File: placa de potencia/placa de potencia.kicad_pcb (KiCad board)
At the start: 2 copper layers, 125 x 121.6 mm, 21 parts, among them J1 XT60-M, J10 B4B-XH-A, J11 B4B-XH-A, J12 B4B-XH-A, J13 B4B-XH-A, J2 XT60-M, J3 B4B-XH-A, J4 XT60-M, J5 B4B-XH-A, J6 B4B-XH-A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

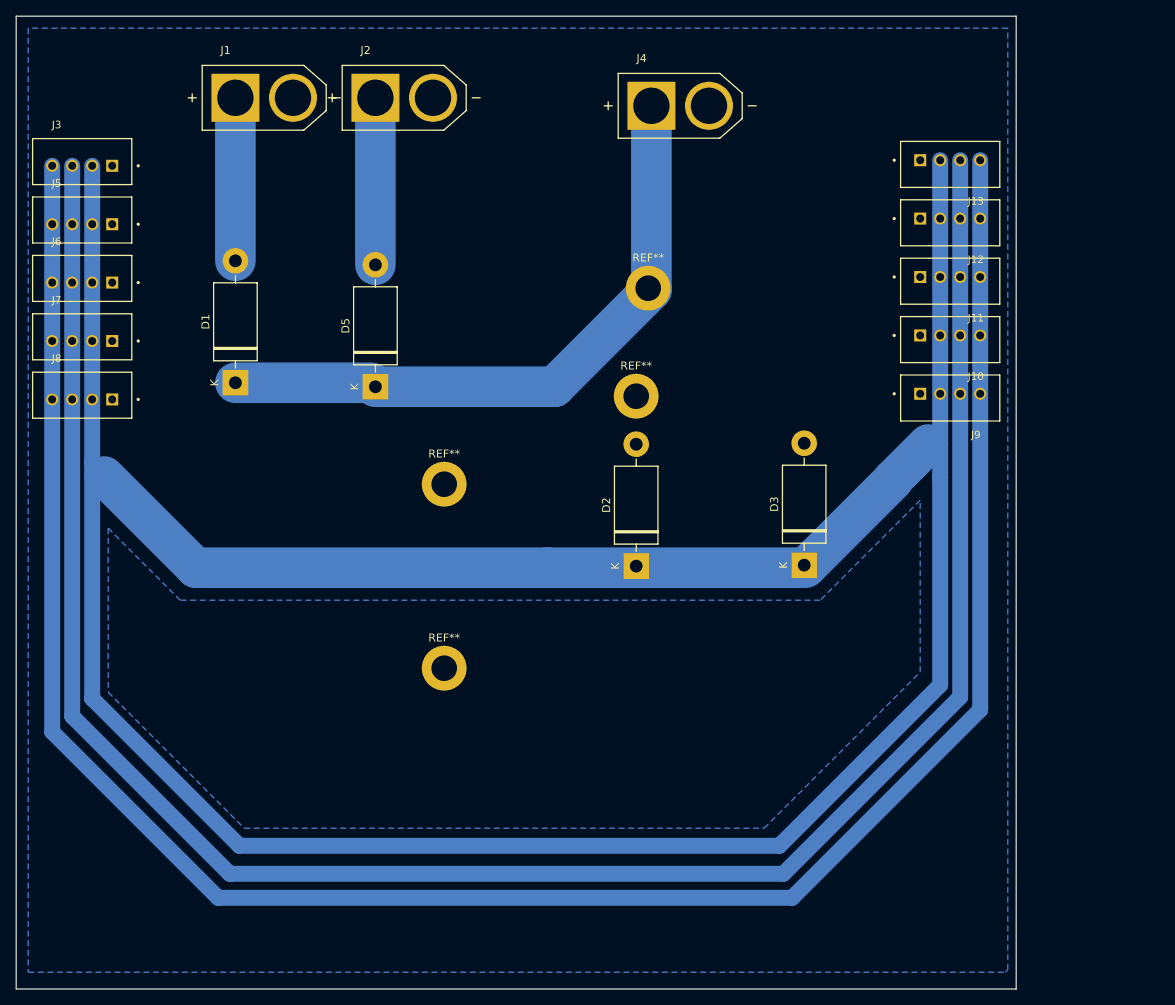
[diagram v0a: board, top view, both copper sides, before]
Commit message: Adionei o arduino na placa integrada (nao terminei) Adicionei a pasta de teclado (projeto pessoal)
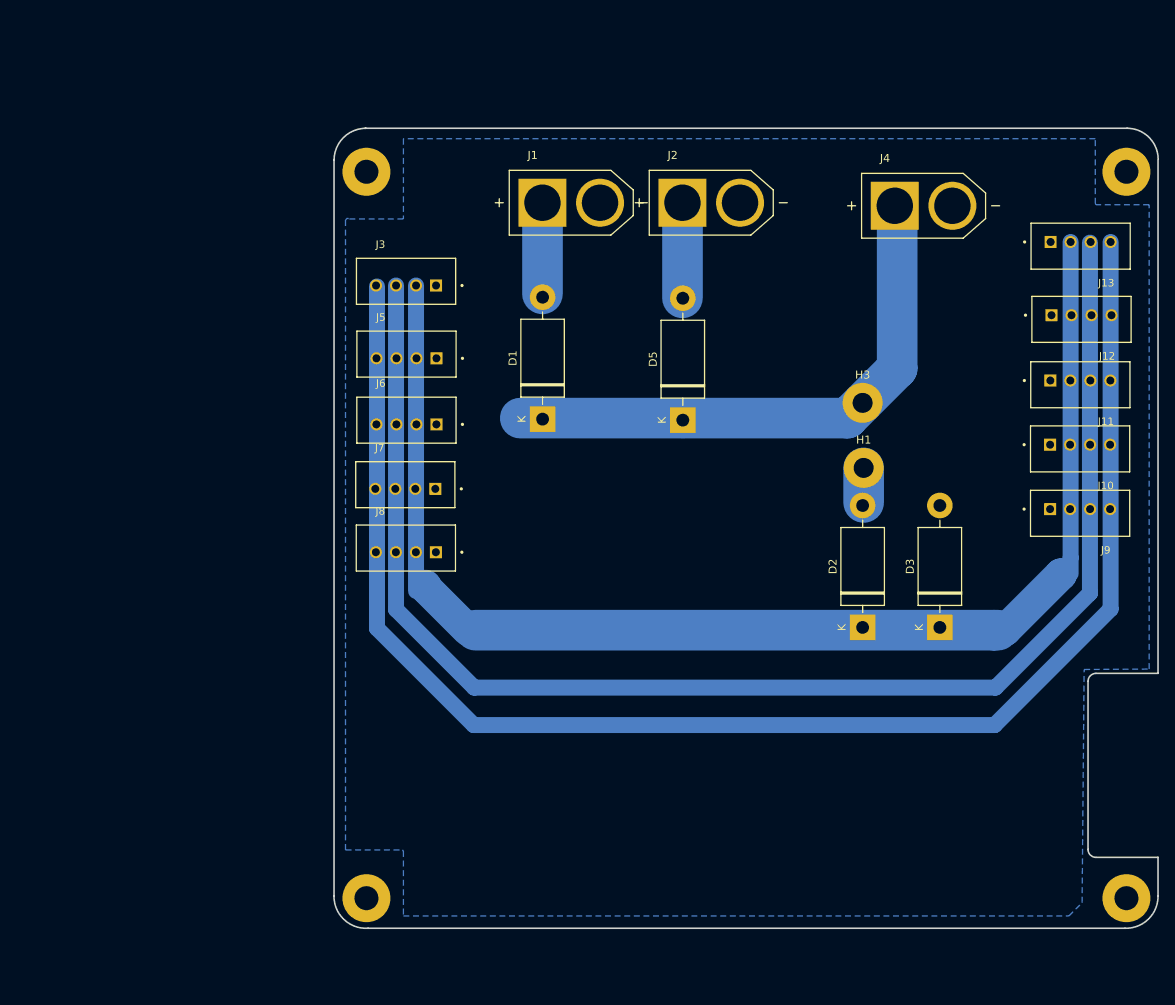
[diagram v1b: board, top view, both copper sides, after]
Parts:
- removed REF** (x4): MountingHole_3.2mm_M3_DIN965_Pad, MountingHole:MountingHole_3.2mm_M3_DIN965_Pad
- added ?: , , F.Cu at (187.3, 47.9)
- added ?: , , F.Cu at (187.3, 138.7)
- added ?: , , F.Cu at (92.3, 138.7)
- added ?: , , F.Cu at (92.3, 47.9)
- added H1: MountingHole_Pad, MountingHole:MountingHole_2.5mm_Pad, F.Cu at (154.4, 85.0)
- added H3: MountingHole_Pad, MountingHole:MountingHole_2.5mm_Pad, F.Cu at (154.3, 76.8)
- moved J8 44.7 mm to (97.2, 95.0)
- moved J7 44.4 mm to (97.1, 87.1)
- moved J6 44.2 mm to (97.3, 79.0)
- moved J5 43.9 mm to (97.3, 70.7)
- moved J3 43.2 mm to (97.2, 61.6)
- moved J1 40.6 mm to (117.9, 51.8)
- moved J2 40.6 mm to (135.4, 51.8)
- moved D1 38.7 mm to (114.3, 78.9)
- moved D5 38.7 mm to (131.8, 79.0)
- moved J4 32.9 mm to (161.9, 52.2)
- moved D2 29.3 mm to (154.3, 104.9)
- moved J9 21.7 mm to (181.5, 90.6)
- moved J10 21.2 mm to (181.5, 82.6)
- moved J11 20.8 mm to (181.5, 74.6)
- moved J12 20.4 mm to (181.7, 66.4)
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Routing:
- net Net-(D2-K): track 368.3 -> 163.2 mm
- net Net-(J10-Pad3): track 264.9 -> 180.1 mm
- net Net-(J10-Pad4): track 273.8 -> 224.9 mm
- net Net-(D1-K): track 79.7 -> 69.8 mm
- net Net-(D5-A): track 21.0 -> 12.0 mm
- net Net-(D1-A): track 20.5 -> 11.5 mm
- net Net-(D2-A): track 0.00 -> 5.40 mm
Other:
- board size 125 x 121.6 mm -> 103 x 100 mm
